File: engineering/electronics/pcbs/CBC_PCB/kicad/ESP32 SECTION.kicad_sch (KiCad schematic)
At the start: 20 parts, among them U2 2.4GHz, U4 1kΩ

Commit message: fix: restore CBC schematic library nicknames
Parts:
- C1: symbol CBC_PCB:HGC0402R5105K250NTEJ -> EasyEDA_Lib:HGC0402R5105K250NTEJ
- C18: symbol CBC_PCB:CL21A475KBQNNNE -> EasyEDA_Lib:CL21A475KBQNNNE
- C19, C22, C24: symbol CBC_PCB:GRM21BR61H106KE43L -> EasyEDA_Lib:GRM21BR61H106KE43L
- C20, C21, C23: symbol CBC_PCB:CC0402KRX7R7BB104 -> EasyEDA_Lib:CC0402KRX7R7BB104
- D3: symbol CBC_PCB:SS14_C7420316 -> EasyEDA_Lib:SS14_C7420316
- D4: symbol CBC_PCB:USBLC6-2SC6 -> EasyEDA_Lib:USBLC6-2SC6
- LED1: symbol CBC_PCB:0603 Green 509-620mcd -> EasyEDA_Lib:0603 Green 509-620mcd
- Q1: symbol CBC_PCB:UMH3N -> EasyEDA_Lib:UMH3N
- R7: symbol CBC_PCB:RT0402BRD0710KL -> EasyEDA_Lib:RT0402BRD0710KL
- R8, R9: symbol CBC_PCB:0402WGF5101TCE -> EasyEDA_Lib:0402WGF5101TCE
- SW1: symbol CBC_PCB:TS-1088-AR02016 -> EasyEDA_Lib:TS-1088-AR02016
- U2: symbol CBC_PCB:ESP32-S3-WROOM-1(N16R8) -> EasyEDA_Lib:ESP32-S3-WROOM-1(N16R8)
- U4: symbol CBC_PCB:MCS0402MC1001FE000 -> EasyEDA_Lib:MCS0402MC1001FE000
- U7: symbol CBC_PCB:CP2104-F03-GM -> EasyEDA_Lib:CP2104-F03-GM
- USB1: symbol CBC_PCB:TYPE-C 16PIN 2MD(073) -> EasyEDA_Lib:TYPE-C 16PIN 2MD(073)
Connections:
- net +3V3: now also C18.2, C19.2, C20.2, C22.2, C23.2, R7.2, U2.2 (3V3), U4.2, U7.5 (VIO), U7.6 (VDD), U7.7 (REGIN)
- net +5V: now also D3.2 (K)
- net CS#1: now also U2.18 (IO10)
- net CS#2: now also U2.22 (IO14)
- net D+: now also D4.6, U7.3 (D+)
- net D-: now also D4.4, U7.4 (D-)
- net DATA1: now also U2.8 (IO15)
- net DATA2: now also U2.7 (IO7)
- net DTR: now also Q1.2 (B), Q1.4 (E), U7.23 (DTR)
- net ESP_ENABLE_SIGNAL: now also U2.6 (IO6)
- net GND: now also C1.1, C18.1, C19.1, C20.1, C21.1, C22.1, C23.1, C24.1, D4.2, LED1.1 (K), R8.1, R9.1, SW1.2, U2.1 (GND), U2.40 (GND), U2.41 (GND), U7.2 (GND), U7.25 (EPAD), USB1.A1B12 (GND), USB1.B1A12 (GND)
- net GPIO0: now also Q1.3 (C), U2.27 (IO0)
- net INT#1: now also U2.23 (IO21)
- net INT#2: now also U2.24 (IO47)
- net MISO: now also U2.21 (IO13)
- net MOSI: now also U2.19 (IO11)
- net PRECHARGE_ESP_SIGNAL: now also U2.4 (IO4)
- net RESET: now also C1.2, Q1.6 (C), R7.1, SW1.1, U2.3 (EN)
- net RESET1: now also U2.25 (IO48)
- net RESET2: now also U2.17 (IO9)
- net RTS: now also Q1.1 (E), Q1.5 (B), U7.19 (RTS)
- net RXD0: now also U2.36 (RXD0), U7.21 (TXD)
- net SCHMITT_OUT: now also U2.5 (IO5)
- net SCK: now also U2.20 (IO12)
- net TXD0: now also U2.37 (TXD0), U7.20 (RXD)
- net USBV: now also C24.2, D3.1 (A), D4.5, U7.8 (VBUS), USB1.A4B9 (VBUS), USB1.B4A9 (VBUS)
- new net: C21.2, USB1.13 (EH), USB1.14 (EH)
- new net: R8.2, USB1.A5 (CC1)
- new net: D4.1, USB1.A6 (Dp1), USB1.B6 (Dp2)
- new net: D4.3, USB1.A7 (Dn1), USB1.B7 (Dn2)
- new net: R9.2, USB1.B5 (CC2)
- new net: LED1.2 (A), U4.1

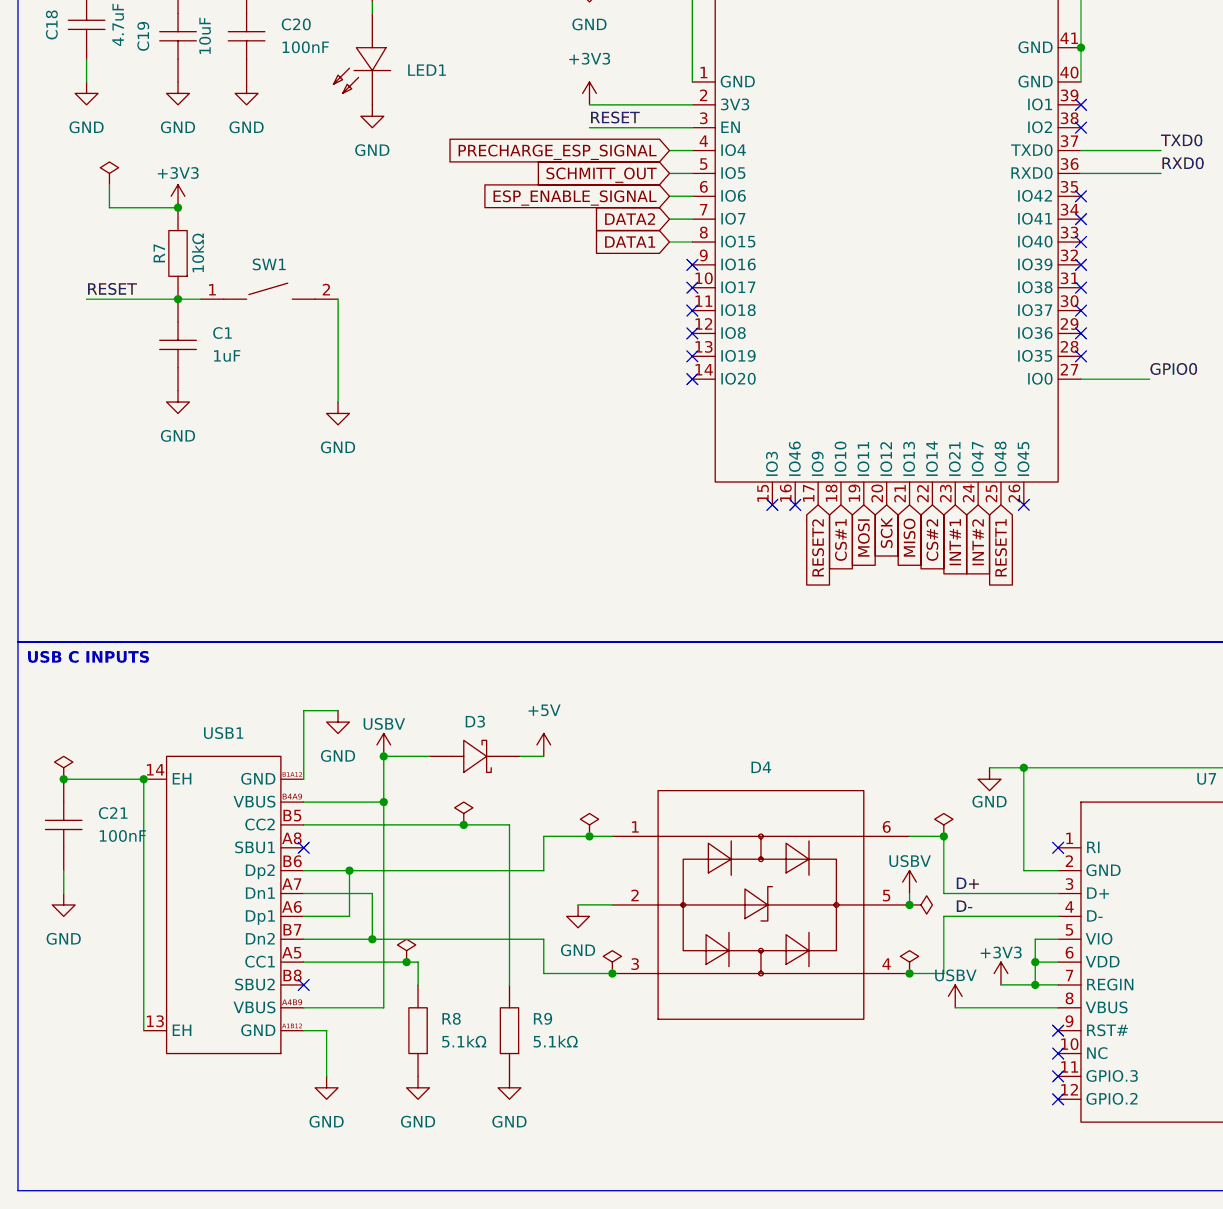
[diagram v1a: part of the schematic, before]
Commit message: fix: assign CBC imported symbol pin types
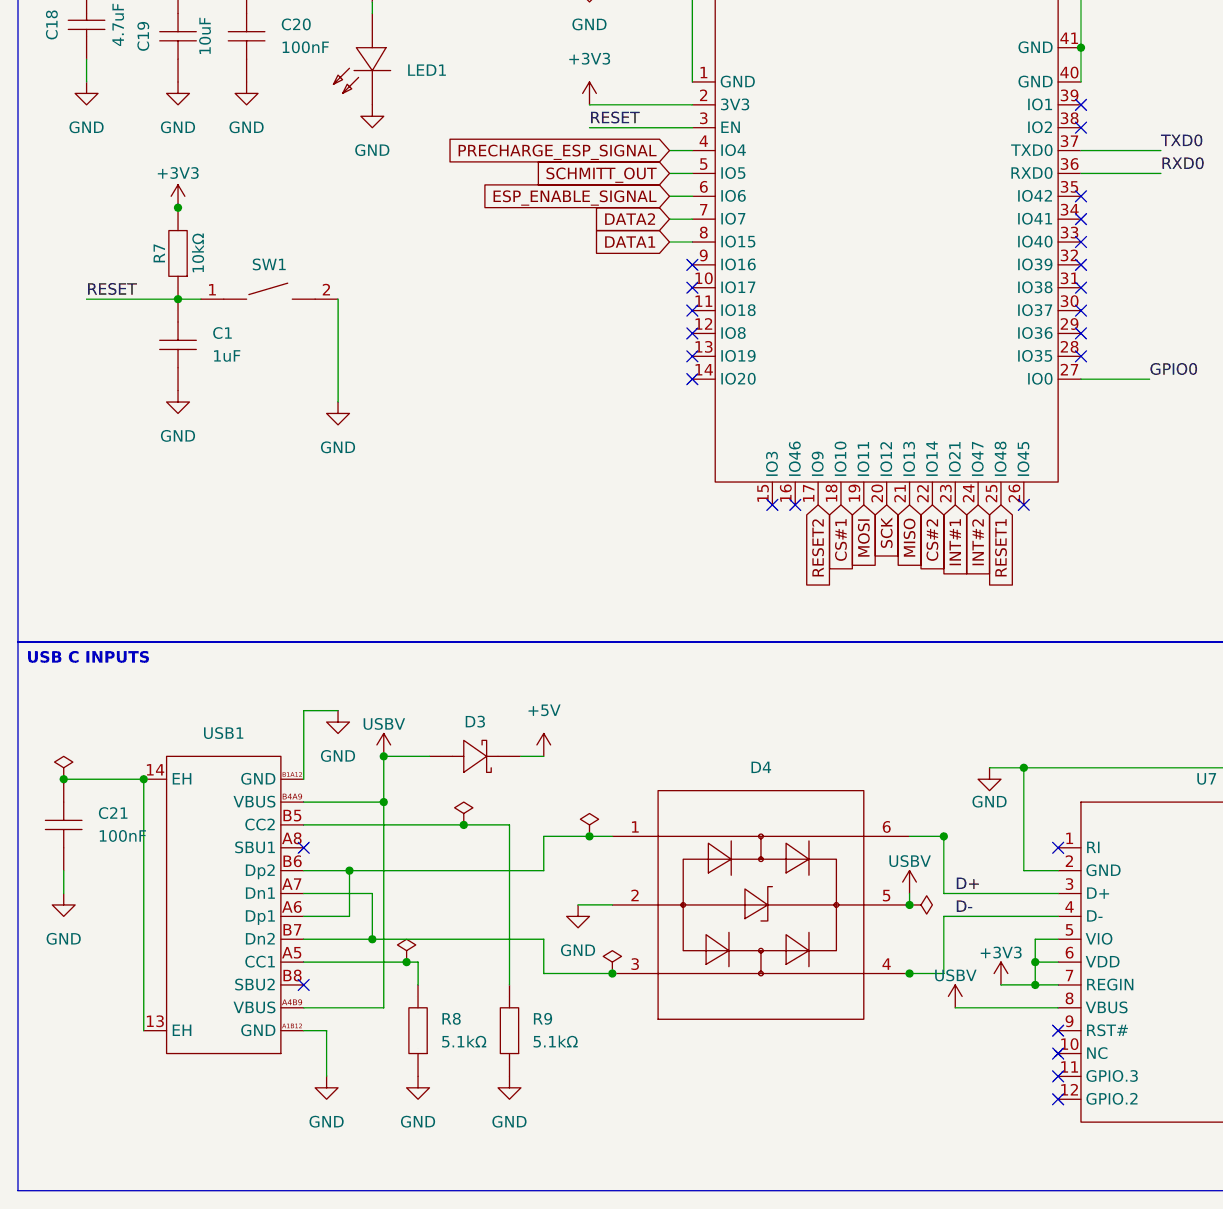
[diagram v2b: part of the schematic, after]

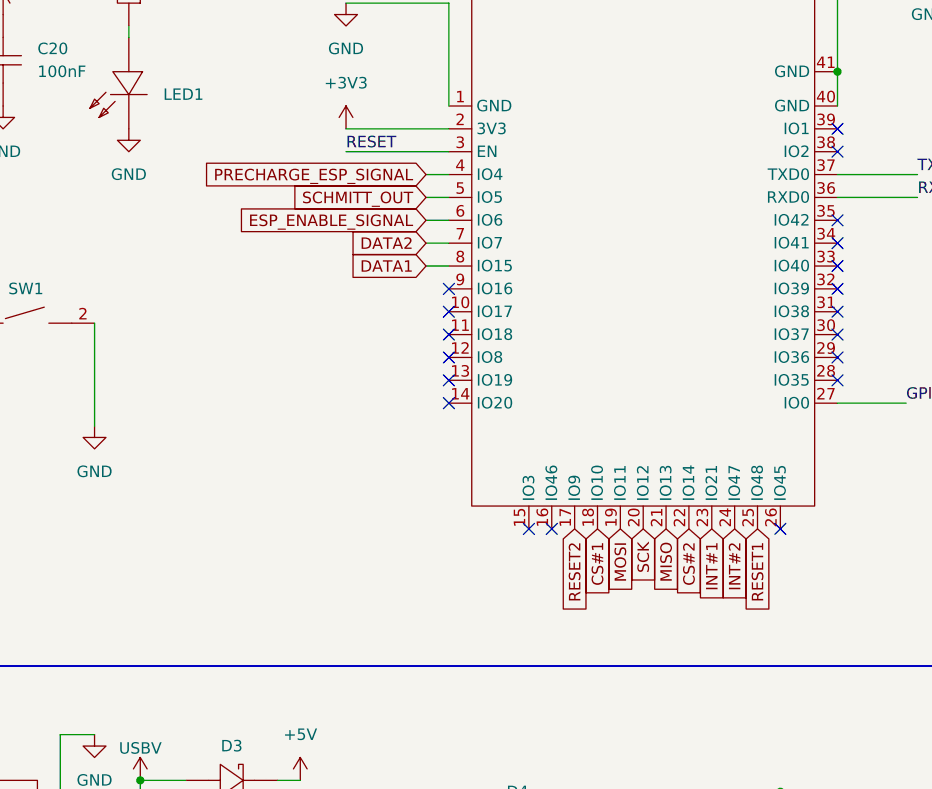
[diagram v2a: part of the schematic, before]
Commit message: docs: capture CBC schematic review follow-ups
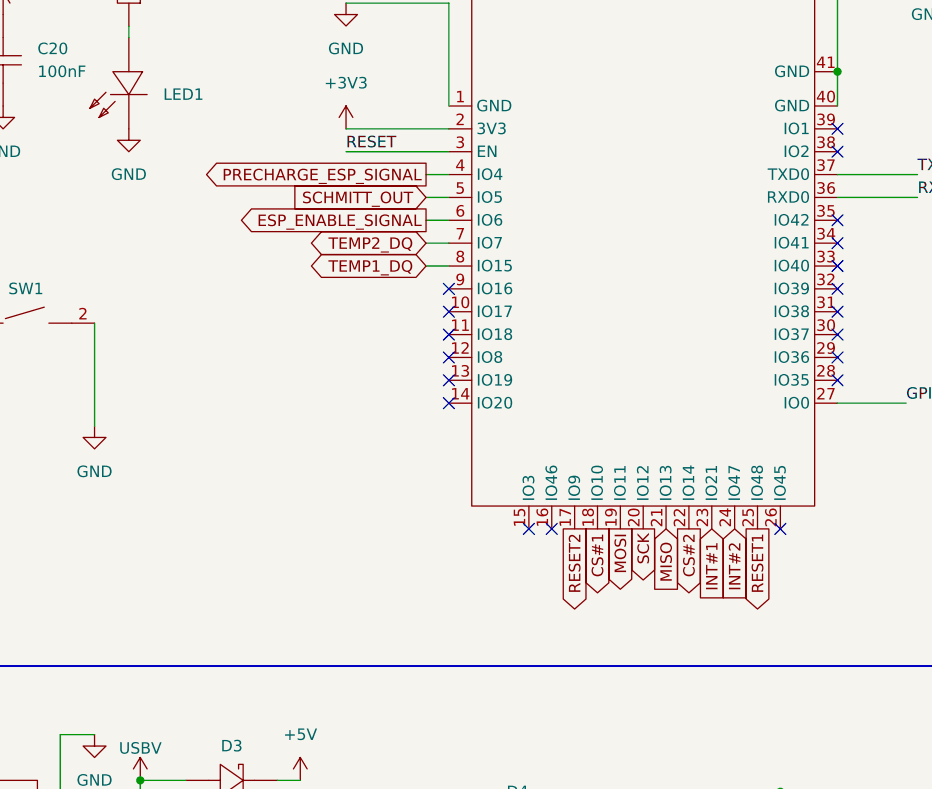
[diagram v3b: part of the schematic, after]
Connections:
- net DATA1 renamed TEMP1_DQ
- net DATA2 renamed TEMP2_DQ
